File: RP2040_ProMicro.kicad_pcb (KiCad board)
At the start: 2 copper layers, 23 x 51 mm, 50 parts, among them J1 HRO_TYPE-C-31-M-14, J2 Conn_01x16, J3 Battery, J6 Conn_01x12, Q1 SI2301A, SW1 SW_Push, SW2 SW_Push, U1 USBLC6-2SC6, U2 SOT23-5 200mA 3.3V, U3 TP4054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

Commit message: Routing in progress
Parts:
- removed C2, C6: 10uF, Capacitor_SMD:C_0402_1005Metric
- removed D1, D3: LED, LED_SMD:LED_1206_3216Metric
- removed F1: 750 mA, Fuse:Fuse_0603_1608Metric
- removed J3: Battery, Connector_JST:JST_EH_S2B-EH_1x02_P2.50mm_Horizontal
- removed J6: Conn_01x12, Connector_PinSocket_2.54mm:PinSocket_1x12_P2.54mm_Vertical
- removed L1: BLM15PX121SN1D, Inductor_SMD:L_0402_1005Metric
- removed Q1: SI2301A, Package_TO_SOT_SMD:SOT-23
- removed R11, R12, R7: 1k, Resistor_SMD:R_0402_1005Metric
- removed R3: 470, Resistor_SMD:R_0402_1005Metric
- removed R6: 2k, Resistor_SMD:R_0402_1005Metric
- removed SW1, SW2: SW_Push, Button_Switch_SMD:SW_Push_SPST_NO_Alps_SKRK
- removed U3: TP4054, Package_TO_SOT_SMD:SOT-23-5
- J2: value Conn_01x16 -> Conn_01x26; footprint Connector_PinSocket_2.54mm:PinSocket_1x16_P2.54mm_Vertical -> mikotofootprints:mikoto-pins
- R10, R9: value 27 -> 27R
- moved R4 30.4 mm to (153.0, 34.8), turned to -90 degrees
- moved D2 29.7 mm to (155.4, 40.3), turned to 0 degrees
- moved J2 27.9 mm to (159.0, 47.9)
- moved C4 27.0 mm to (153.2, 44.3)
- moved C5 27.0 mm to (153.2, 46.4)
- moved C3 25.5 mm to (153.0, 39.8)
- moved R5 24.0 mm to (153.2, 42.2)
- moved U2 22.0 mm to (155.6, 43.4)
- moved C19 19.6 mm to (153.5, 54.3), turned to 0 degrees
- moved C11 18.5 mm to (155.3, 56.4)
- moved J1 16.0 mm to (159.0, 33.9)
- moved U1 15.8 mm to (159.1, 41.3)
- moved C1 15.3 mm to (153.0, 37.7)
- moved R2 14.9 mm to (153.0, 32.6), turned to 90 degrees
- moved C14 14.0 mm to (164.6, 49.5), turned to 180 degrees
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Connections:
- C1 pad 1: GND -> +5V
- C1 pad 2: +5V -> GND
- J1 pad A4: VBUS -> +5V
- J1 pad A9: VBUS -> +5V
- J1 pad B4: VBUS -> +5V
- J1 pad B9: VBUS -> +5V
- J2 pad 1: GND -> +5V
- J2 pad 10: /GPIO5 -> unconnected-(J2-Pad10)
- J2 pad 11: /GPIO4 -> unconnected-(J2-Pad11)
- J2 pad 12: /GPIO3 -> unconnected-(J2-Pad12)
- J2 pad 13: /GPIO2 -> unconnected-(J2-Pad13)
- J2 pad 14: /GPIO1 -> unconnected-(J2-Pad14)
- J2 pad 15: /GPIO0 -> unconnected-(J2-Pad15)
- J2 pad 16: +3V3 -> unconnected-(J2-Pad16)
- J2 pad 2: /GPIO14 -> unconnected-(J2-Pad2)
- J2 pad 3: /GPIO13 -> unconnected-(J2-Pad3)
- J2 pad 4: /GPIO12 -> GND
- J2 pad 5: /GPIO11 -> GND
- J2 pad 6: /GPIO10 -> unconnected-(J2-Pad6)
- J2 pad 7: /GPIO9 -> unconnected-(J2-Pad7)
- J2 pad 8: /GPIO8 -> unconnected-(J2-Pad8)
- J2 pad 9: /GPIO6 -> unconnected-(J2-Pad9)
- U1 pad 1: D+ -> D-
- U1 pad 3: D- -> D+
- U1 pad 4: USB_D- -> USB_D+
- U1 pad 6: USB_D+ -> USB_D-
- U4 pad 26: +3V3 -> /RESET
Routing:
- net +3V3: track 159.9 -> 69.4 mm, vias 7 -> 8
- net +BATT: track 29.1 -> 0.00 mm, vias 1 -> 0
- net +5V: track 51.6 -> 23.0 mm, vias 4 -> 0
- net QSPI_SS: track 40.8 -> 14.1 mm
- net VBUS: track 22.6 -> 0.00 mm
- net /GPIO14: track 21.4 -> 0.00 mm
- net /GPIO13: track 18.7 -> 0.00 mm
- net unconnected-(J1-PadS1): track 17.3 -> 0.00 mm
- net /GPIO26: track 17.4 -> 0.67 mm, vias 0 -> 1
- net /GPIO12: track 15.8 -> 0.00 mm
- net Net-(R7-Pad1): track 15.3 -> 0.00 mm, vias 2 -> 0
- net /GPIO1: track 15.1 -> 0.00 mm
- net /GPIO0: track 15.1 -> 0.00 mm
- net /GPIO25: track 15.2 -> 0.67 mm, vias 0 -> 1
- net USB_D+: track 31.2 -> 16.8 mm
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- added copper zone on F.Cu, net +3V3
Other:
- board size 23 x 51 mm -> 18 x 33.5 mm

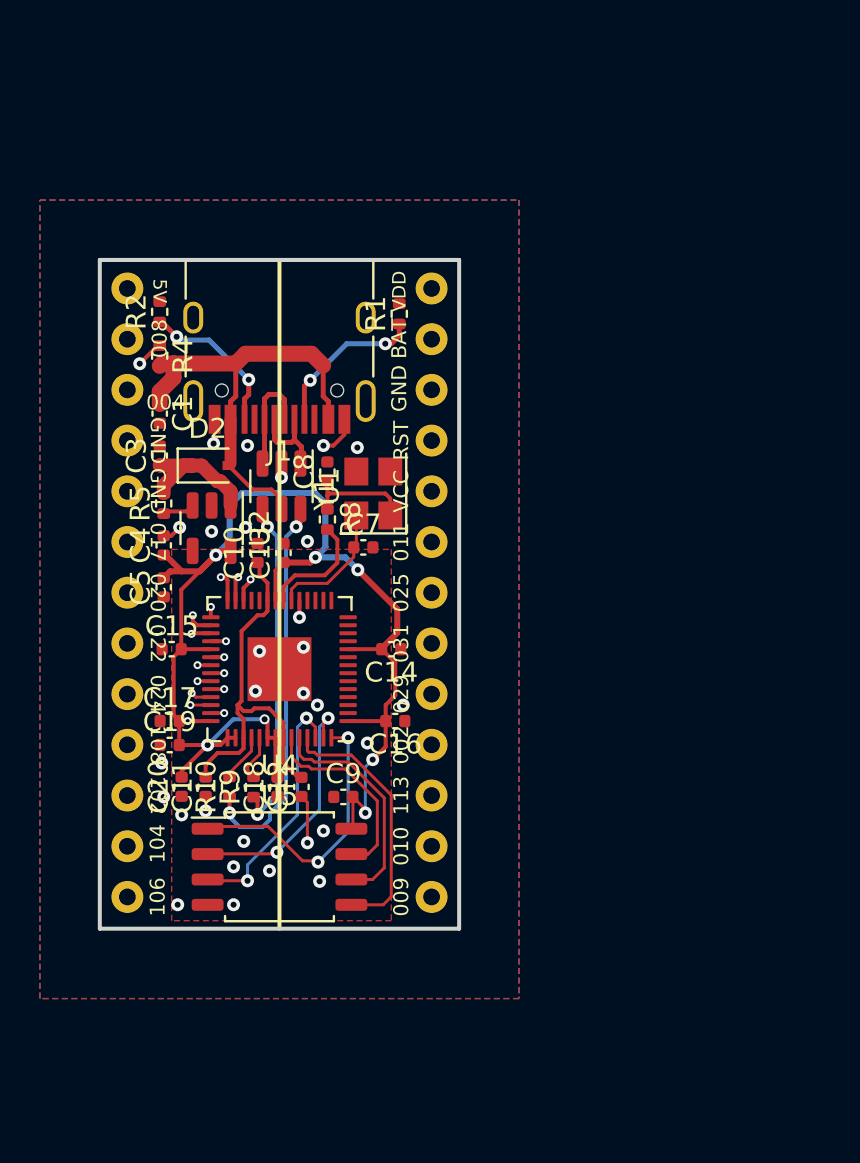
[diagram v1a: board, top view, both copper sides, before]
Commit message: added more vias around crystal
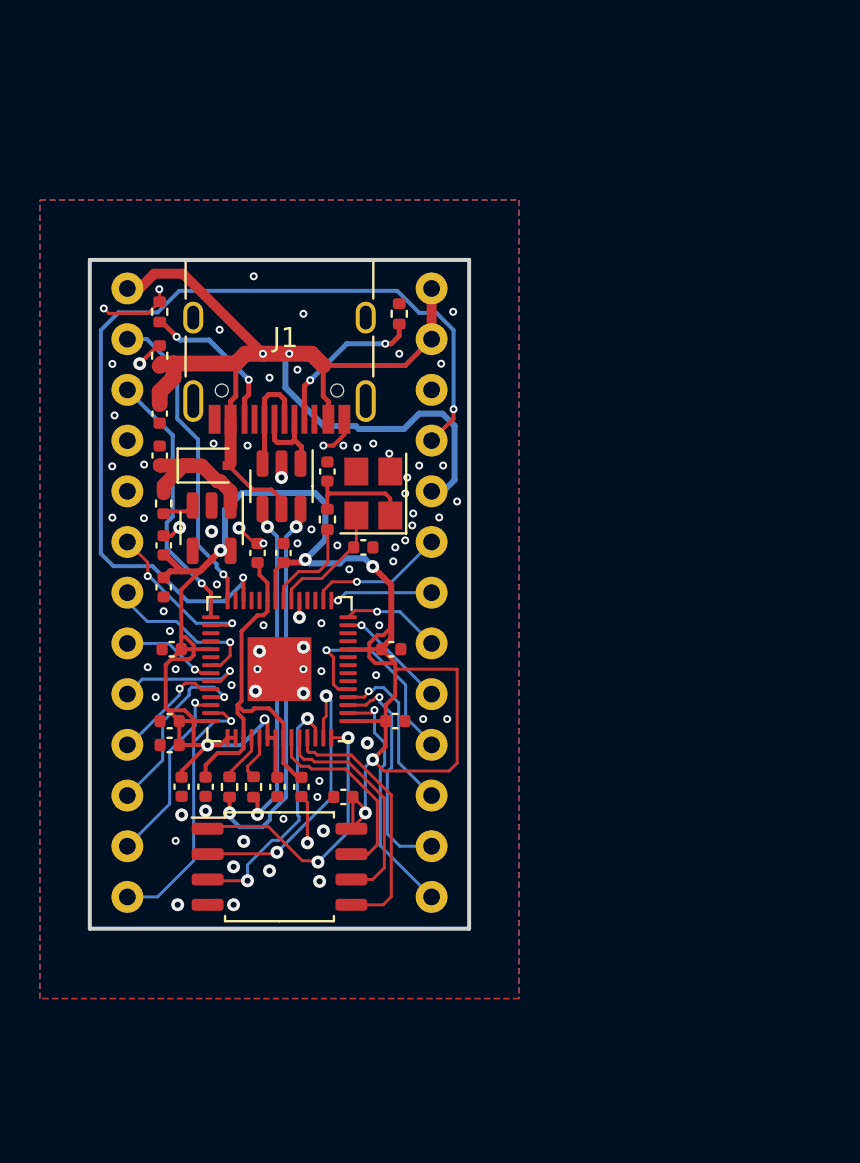
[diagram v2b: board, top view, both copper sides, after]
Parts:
- J2: footprint mikotofootprints:mikoto-pins -> mikotofootprints:promicrorp2040
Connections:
- J2 pad 10: unconnected-(J2-Pad10) -> /GPIO26
- J2 pad 11: unconnected-(J2-Pad11) -> /GPIO27
- J2 pad 12: unconnected-(J2-Pad12) -> /GPIO28
- J2 pad 13: unconnected-(J2-Pad13) -> /GPIO29
- J2 pad 14: unconnected-(J2-Pad14) -> /GPIO0
- J2 pad 15: unconnected-(J2-Pad15) -> /GPIO1
- J2 pad 16: unconnected-(J2-Pad16) -> /GPIO2
- J2 pad 17: unconnected-(J2-Pad17) -> /GPIO3
- J2 pad 18: unconnected-(J2-Pad18) -> /GPIO10
- J2 pad 19: unconnected-(J2-Pad19) -> /GPIO11
- J2 pad 2: unconnected-(J2-Pad2) -> /GPIO17
- J2 pad 20: unconnected-(J2-Pad20) -> /GPIO12
- J2 pad 21: unconnected-(J2-Pad21) -> /GPIO13
- J2 pad 3: unconnected-(J2-Pad3) -> /GPIO18
- J2 pad 6: unconnected-(J2-Pad6) -> /GPIO19
- J2 pad 7: unconnected-(J2-Pad7) -> /GPIO23
- J2 pad 8: unconnected-(J2-Pad8) -> /GPIO24
- J2 pad 9: unconnected-(J2-Pad9) -> /GPIO25
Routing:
- net /RESET: track 1.21 -> 46.4 mm, vias 1 -> 2
- net +5V: track 23.0 -> 57.3 mm, vias 0 -> 2
- net +3V3: track 69.4 -> 93.4 mm, vias 8 -> 7
- net /GPIO17: track 1.42 -> 15.7 mm
- net /GPIO18: track 0.52 -> 13.4 mm
- net /GPIO29: track 0.67 -> 13.5 mm
- net /GPIO0: track 0.00 -> 12.1 mm, vias 0 -> 1
- net /GPIO1: track 0.00 -> 11.4 mm, vias 0 -> 1
- net /GPIO3: track 0.00 -> 10.9 mm, vias 0 -> 1
- net /GPIO2: track 0.00 -> 8.42 mm, vias 0 -> 1
- net /GPIO28: track 1.03 -> 9.44 mm
- net /GPIO27: track 1.05 -> 9.27 mm
- net /GPIO23: track 0.67 -> 8.28 mm
- net /GPIO19: track 1.29 -> 8.45 mm, vias 1 -> 2
- net /GPIO13: track 0.00 -> 6.93 mm, vias 0 -> 1
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- removed copper zone on F.Cu, net +3V3
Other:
- board size 18 x 33.5 mm -> 19 x 33.5 mm
- board text added: "17"
